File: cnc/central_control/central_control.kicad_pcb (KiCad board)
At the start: 2 copper layers, 64 x 107 mm, 113 parts, among them J1 DE9_Receptacle, J2 AVR-UPDI, J3 7pins, J4 Phoenix, J5 6pins, J6 6pins, J7 6pins, J8 3pins, J9 4pins, Q1 BSS138, U1 ATtiny1626-S, U10 PC817, U2 PC817, U3 PC817, U4 PCA9555PW, U5 LT1785AxS8, U7 LMR33630ADDA, U8 PC817, U9 PCA9555PW

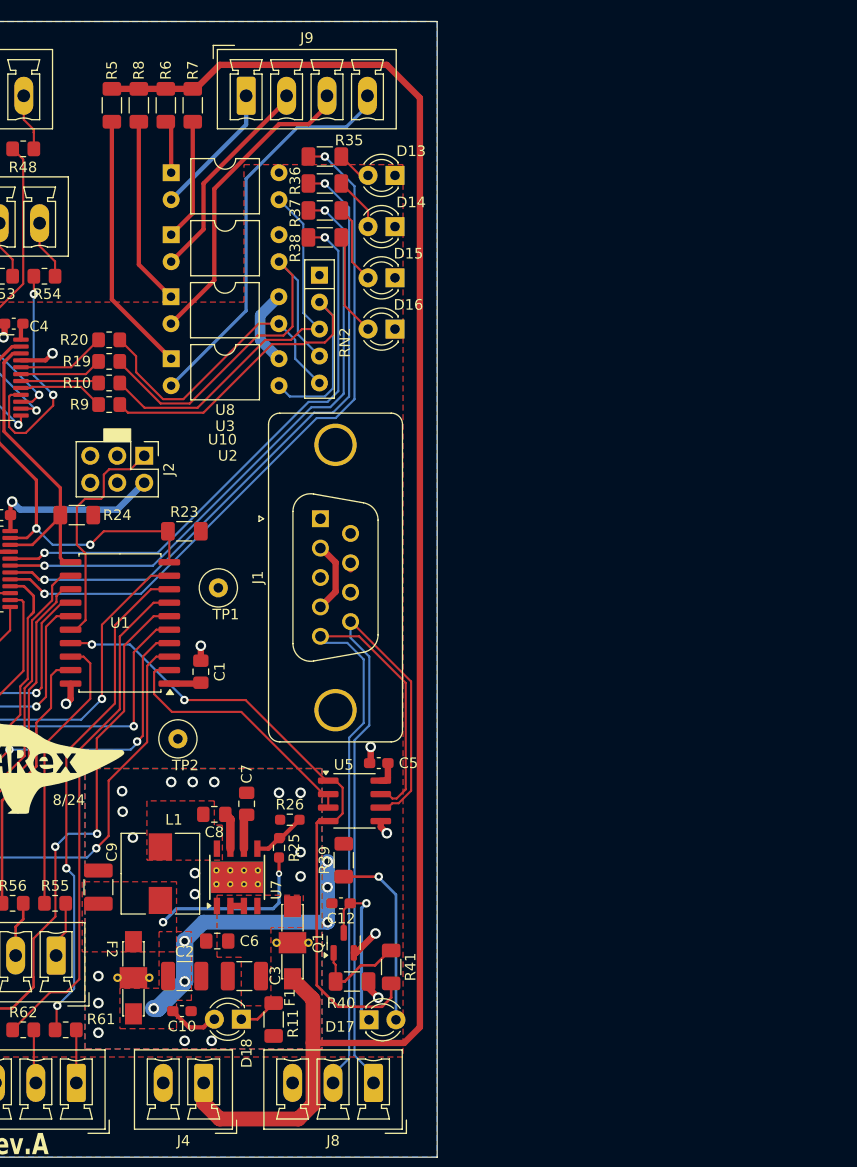
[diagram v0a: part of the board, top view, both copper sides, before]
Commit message: Split sheets
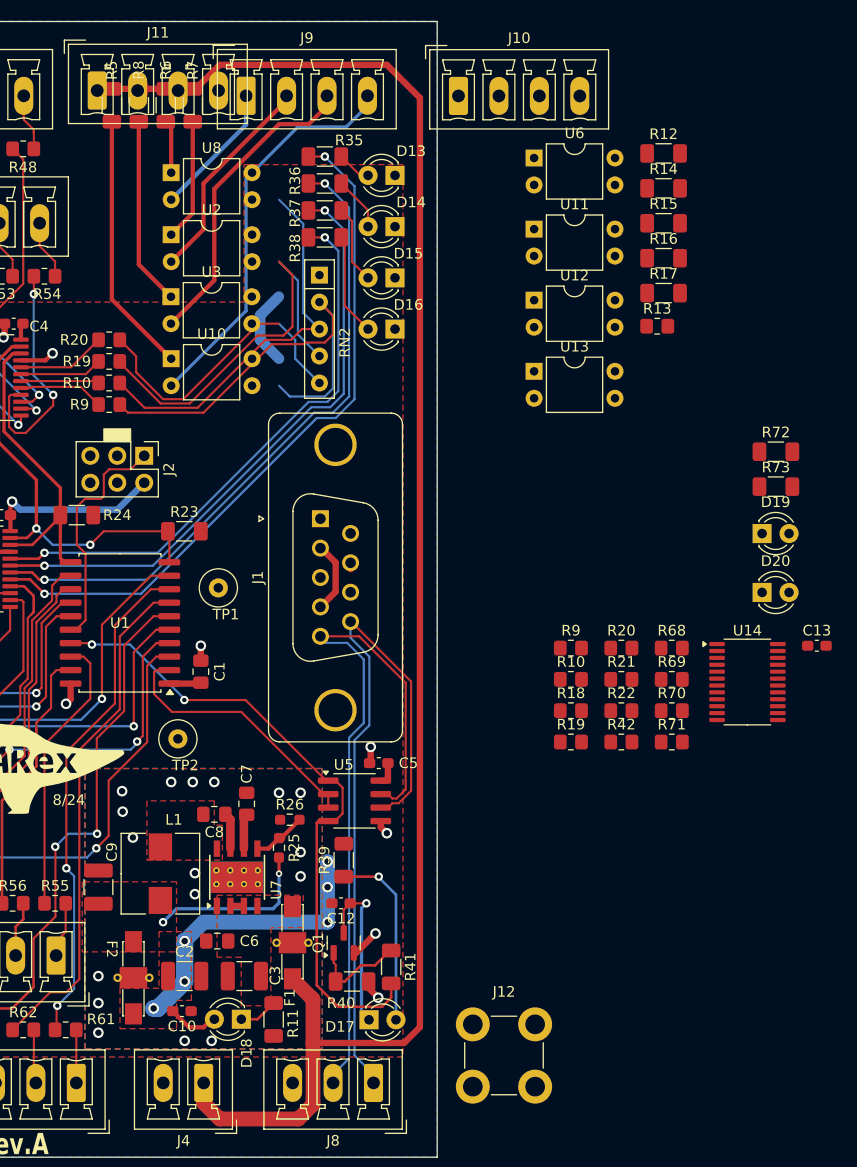
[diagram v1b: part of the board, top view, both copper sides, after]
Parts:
- added C13: 100n, Capacitor_SMD:C_0603_1608Metric_Pad1.08x0.95mm_HandSolder, F.Cu at (199.8, 107.8)
- added D19: LED, LED_THT:LED_D3.0mm, F.Cu at (194.6, 97.2)
- added D20: LED, LED_THT:LED_D3.0mm, F.Cu at (194.6, 102.8)
- added J10: 4pins, Connector_Phoenix_MC:PhoenixContact_MCV_1,5_4-G-3.81_1x04_P3.81mm_Vertical, F.Cu at (166.0, 56.0)
- added J11: Screw_Terminal_01x04, Connector_Phoenix_MC:PhoenixContact_MCV_1,5_4-G-3.81_1x04_P3.81mm_Vertical, F.Cu at (132.0, 55.5)
- added J12: Screw_Terminal_01x01, TerminalBlock_Wuerth:Wuerth_REDCUBE-THR_WP-THRBU_74650173_THR, F.Cu at (170.3, 146.4)
- added R10: 332, Resistor_SMD:R_0805_2012Metric_Pad1.20x1.40mm_HandSolder, F.Cu at (176.6, 111.0)
- added R12: 100K, Resistor_SMD:R_1206_3216Metric_Pad1.30x1.75mm_HandSolder, F.Cu at (185.3, 61.4)
- added R13: 332, Resistor_SMD:R_0805_2012Metric_Pad1.20x1.40mm_HandSolder, F.Cu at (184.7, 77.7)
- added R14: 3k32, Resistor_SMD:R_1206_3216Metric_Pad1.30x1.75mm_HandSolder, F.Cu at (185.3, 64.7)
- added R15: 3k32, Resistor_SMD:R_1206_3216Metric_Pad1.30x1.75mm_HandSolder, F.Cu at (185.3, 68.0)
- added R16: 3k32, Resistor_SMD:R_1206_3216Metric_Pad1.30x1.75mm_HandSolder, F.Cu at (185.3, 71.3)
- added R17: 3k32, Resistor_SMD:R_1206_3216Metric_Pad1.30x1.75mm_HandSolder, F.Cu at (185.3, 74.6)
- added R18: 332, Resistor_SMD:R_0805_2012Metric_Pad1.20x1.40mm_HandSolder, F.Cu at (176.6, 113.9)
- added R19: 332, Resistor_SMD:R_0805_2012Metric_Pad1.20x1.40mm_HandSolder, F.Cu at (176.6, 116.9)
- added R20: 332, Resistor_SMD:R_0805_2012Metric_Pad1.20x1.40mm_HandSolder, F.Cu at (181.4, 108.0)
- added R21: 332, Resistor_SMD:R_0805_2012Metric_Pad1.20x1.40mm_HandSolder, F.Cu at (181.4, 111.0)
- added R22: 332, Resistor_SMD:R_0805_2012Metric_Pad1.20x1.40mm_HandSolder, F.Cu at (181.4, 113.9)
- added R42: 332, Resistor_SMD:R_0805_2012Metric_Pad1.20x1.40mm_HandSolder, F.Cu at (181.4, 116.9)
- added R68: 332, Resistor_SMD:R_0805_2012Metric_Pad1.20x1.40mm_HandSolder, F.Cu at (186.1, 108.0)
- added R69: 332, Resistor_SMD:R_0805_2012Metric_Pad1.20x1.40mm_HandSolder, F.Cu at (186.1, 111.0)
- added R70: 332, Resistor_SMD:R_0805_2012Metric_Pad1.20x1.40mm_HandSolder, F.Cu at (186.1, 113.9)
- added R71: 332, Resistor_SMD:R_0805_2012Metric_Pad1.20x1.40mm_HandSolder, F.Cu at (186.1, 116.9)
- added R72: 432, Resistor_SMD:R_1206_3216Metric_Pad1.30x1.75mm_HandSolder, F.Cu at (195.9, 89.5)
- added R73: 432, Resistor_SMD:R_1206_3216Metric_Pad1.30x1.75mm_HandSolder, F.Cu at (195.9, 92.8)
- added R9: 332, Resistor_SMD:R_0805_2012Metric_Pad1.20x1.40mm_HandSolder, F.Cu at (176.6, 108.0)
- added U11: PC817, Package_DIP:DIP-4_W7.62mm, F.Cu at (173.1, 68.6)
- added U12: PC817, Package_DIP:DIP-4_W7.62mm, F.Cu at (173.1, 75.3)
- added U13: PC817, Package_DIP:DIP-4_W7.62mm, F.Cu at (173.1, 82.0)
- added U14: PCA9555PW, Package_SO:TSSOP-24_4.4x7.8mm_P0.65mm, F.Cu at (193.2, 111.2)
- added U6: PC817, Package_DIP:DIP-4_W7.62mm, F.Cu at (173.1, 61.9)
- U10, U2, U3, U8: footprint Package_DIP:DIP-4_W10.16mm -> Package_DIP:DIP-4_W7.62mm
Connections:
- net /VIN renamed /VDD
- J1 pad 2: VDD -> +24V
- J1 pad 4: VDD -> +24V
- U1 pad 12: /MSO_OUT9 -> Net-(U1-PC0)
- U1 pad 13: /MSO_OUT10 -> Net-(U1-PC1)
- U1 pad 14: /MSO_OUT11 -> Net-(U1-PC2)
- U1 pad 15: /MSO_OUT12 -> Net-(U1-PC3)
- U1 pad 17: TXD -> Net-(U1-PA1)
- U1 pad 18: /MSO_OUT0 -> Net-(U1-PA2)
- U1 pad 19: /MSO_OUT1 -> Net-(U1-PA3)
- U1 pad 3: /MSO_OUT2 -> unconnected-(U1-PA5-Pad3)
- U1 pad 4: /MSO_OUT3 -> unconnected-(U1-PA6-Pad4)
- U1 pad 5: /MSO_OUT4 -> unconnected-(U1-PA7-Pad5)
- U1 pad 6: /MSO_OUT8 -> Net-(U1-PB5)
- U1 pad 7: /MSO_OUT7 -> Net-(U1-PB4)
- U1 pad 8: /MSO_OUT6 -> Net-(U1-PB3)
- U1 pad 9: /MSO_OUT5 -> Net-(U1-PB2)
- U4 pad 17: Net-(U4-IO1_4) -> unconnected-(U4-IO1_4-Pad17)
- U4 pad 18: Net-(U4-IO1_5) -> unconnected-(U4-IO1_5-Pad18)
- U4 pad 19: Net-(U4-IO1_6) -> unconnected-(U4-IO1_6-Pad19)
- U4 pad 20: Net-(U4-IO1_7) -> unconnected-(U4-IO1_7-Pad20)
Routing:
- net DOOR_DOWN: track 28.3 -> 35.6 mm
- net VCC: track 63.4 -> 56.1 mm
- net +24V: track 155.2 -> 161.9 mm
- net VDD: track 6.69 -> 0.00 mm

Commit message: On-going
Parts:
- removed C11: 100n, Capacitor_SMD:C_0603_1608Metric_Pad1.08x0.95mm_HandSolder
- removed D19, D20: LED, LED_THT:LED_D3.0mm
- removed J3: 7pins, Connector_Phoenix_MC:PhoenixContact_MCV_1,5_7-G-3.81_1x07_P3.81mm_Vertical
- removed J4: Phoenix, Connector_Phoenix_MC:PhoenixContact_MCV_1,5_2-G-3.81_1x02_P3.81mm_Vertical
- removed J5: 6pins, Connector_Phoenix_MC:PhoenixContact_MCV_1,5_6-G-3.81_1x06_P3.81mm_Vertical
- removed J9: 4pins, Connector_Phoenix_MC:PhoenixContact_MCV_1,5_4-G-3.81_1x04_P3.81mm_Vertical
- removed Q1: BSS138, Package_TO_SOT_SMD:SOT-23
- removed R23: 2k21, Resistor_SMD:R_1206_3216Metric_Pad1.30x1.75mm_HandSolder
- removed R73: 432, Resistor_SMD:R_1206_3216Metric_Pad1.30x1.75mm_HandSolder
- removed RN2: R_Network04, Resistor_THT:R_Array_SIP5
- removed U14, U4: PCA9555PW, Package_SO:TSSOP-24_4.4x7.8mm_P0.65mm
- added C14: 100n, Capacitor_SMD:C_0603_1608Metric_Pad1.08x0.95mm_HandSolder, F.Cu at (385.7, 167.1)
- added J13: 3pins, Connector_Phoenix_MC:PhoenixContact_MCV_1,5_3-G-3.81_1x03_P3.81mm_Vertical, F.Cu at (177.5, 148.8)
- added J14: DE9_Receptacle, Connector_Dsub:DSUB-9_Socket_Vertical_P2.77x2.84mm_MountingHoles, F.Cu at (192.8, 84.7)
- added J17: Phoenix, Connector_Phoenix_MC:PhoenixContact_MCV_1,5_2-G-3.81_1x02_P3.81mm_Vertical, F.Cu at (134.4, 148.8)
- added J18: Phoenix, Connector_Phoenix_MC:PhoenixContact_MCV_1,5_2-G-3.81_1x02_P3.81mm_Vertical, F.Cu at (130.6, 56.1)
- added J19: 7pins, Connector_Phoenix_MC:PhoenixContact_MCV_1,5_7-G-3.81_1x07_P3.81mm_Vertical, F.Cu at (136.9, 67.8)
- added J20: 3pins, Connector_Phoenix_MC:PhoenixContact_MCV_1,5_3-G-3.81_1x03_P3.81mm_Vertical, F.Cu at (190.2, 56.1)
- added J21: 3pins, Connector_Phoenix_MC:PhoenixContact_MCV_1,5_3-G-3.81_1x03_P3.81mm_Vertical, F.Cu at (176.3, 56.1)
- added J22: Phoenix, Connector_Phoenix_MC:PhoenixContact_MCV_1,5_2-G-3.81_1x02_P3.81mm_Vertical, F.Cu at (166.1, 56.1)
- added J23: 3pins, Connector_Phoenix_MC:PhoenixContact_MCV_1,5_3-G-3.81_1x03_P3.81mm_Vertical, F.Cu at (166.1, 67.8)
- added J24: 3pins, Connector_Phoenix_MC:PhoenixContact_MCV_1,5_3-G-3.81_1x03_P3.81mm_Vertical, F.Cu at (122.9, 67.8)
- added RN1: 10k, Resistor_THT:R_Array_SIP5, F.Cu at (361.9, 168.0)
- added TP3: IDLE, TestPoint:TestPoint_Loop_D3.50mm_Drill0.9mm_Beaded, F.Cu at (378.9, 168.5)
- C1: value 1u -> 10u 50v; footprint Capacitor_SMD:C_0805_2012Metric_Pad1.18x1.45mm_HandSolder -> Capacitor_SMD:C_1210_3225Metric_Pad1.33x2.70mm_HandSolder
- C10: value 100n -> 1u; footprint Capacitor_SMD:C_0603_1608Metric_Pad1.08x0.95mm_HandSolder -> Capacitor_SMD:C_0805_2012Metric_Pad1.18x1.45mm_HandSolder
- C12: value 1u -> 100n
- C2: value 47u -> 220nF; footprint Capacitor_SMD:C_1210_3225Metric_Pad1.33x2.70mm_HandSolder -> Capacitor_SMD:C_0805_2012Metric_Pad1.18x1.45mm_HandSolder
- C3: value 10u 50v -> 1u; footprint Capacitor_SMD:C_1210_3225Metric_Pad1.33x2.70mm_HandSolder -> Capacitor_SMD:C_0805_2012Metric_Pad1.18x1.45mm_HandSolder
- C4: value 100n -> 10n; footprint Capacitor_SMD:C_0603_1608Metric_Pad1.08x0.95mm_HandSolder -> Capacitor_SMD:C_0805_2012Metric_Pad1.18x1.45mm_HandSolder
- C5: value 100n -> 10u 50v; footprint Capacitor_SMD:C_0603_1608Metric_Pad1.08x0.95mm_HandSolder -> Capacitor_SMD:C_1210_3225Metric_Pad1.33x2.70mm_HandSolder
- C6: value 220nF -> 47u; footprint Capacitor_SMD:C_0805_2012Metric_Pad1.18x1.45mm_HandSolder -> Capacitor_SMD:C_1210_3225Metric_Pad1.33x2.70mm_HandSolder
- C7: value 1u -> 100n; footprint Capacitor_SMD:C_0805_2012Metric_Pad1.18x1.45mm_HandSolder -> Capacitor_SMD:C_0603_1608Metric_Pad1.08x0.95mm_HandSolder
- C8: value 10n -> 100n; footprint Capacitor_SMD:C_0805_2012Metric_Pad1.18x1.45mm_HandSolder -> Capacitor_SMD:C_0603_1608Metric_Pad1.08x0.95mm_HandSolder
- C9: value 10u 50v -> 100n; footprint Capacitor_SMD:C_1210_3225Metric_Pad1.33x2.70mm_HandSolder -> Capacitor_SMD:C_0805_2012Metric_Pad1.18x1.45mm_HandSolder
- D2: value LED -> red
- D3: value LED -> orange
- D4: value LED -> green
- D5: value LED -> GRN
- J1: value DE9_Receptacle -> AVR-UPDI; footprint Connector_Dsub:DSUB-9_Female_Vertical_P2.77x2.84mm_MountingHoles -> Connector_PinHeader_2.54mm:PinHeader_2x03_P2.54mm_Vertical
- J10: value 4pins -> Screw_Terminal_01x01; footprint Connector_Phoenix_MC:PhoenixContact_MCV_1,5_4-G-3.81_1x04_P3.81mm_Vertical -> adarwoo:GroundPlot
- J11: value Screw_Terminal_01x04 -> 6pins; footprint Connector_Phoenix_MC:PhoenixContact_MCV_1,5_4-G-3.81_1x04_P3.81mm_Vertical -> Connector_Phoenix_MC:PhoenixContact_MCV_1,5_6-G-3.81_1x06_P3.81mm_Vertical
- J12: value Screw_Terminal_01x01 -> 7pins; footprint TerminalBlock_Wuerth:Wuerth_REDCUBE-THR_WP-THRBU_74650173_THR -> Connector_Phoenix_MC:PhoenixContact_MCV_1,5_7-G-3.81_1x07_P3.81mm_Vertical
- J2: value AVR-UPDI -> Screw_Terminal_01x04; footprint Connector_PinHeader_2.54mm:PinHeader_2x03_P2.54mm_Vertical -> Connector_Phoenix_MC:PhoenixContact_MCV_1,5_4-G-3.81_1x04_P3.81mm_Vertical
- J6: value 6pins -> Phoenix; footprint Connector_Phoenix_MC:PhoenixContact_MCV_1,5_6-G-3.81_1x06_P3.81mm_Vertical -> Connector_Phoenix_MC:PhoenixContact_MCV_1,5_2-G-3.81_1x02_P3.81mm_Vertical
- J8: value 3pins -> 6pins; footprint Connector_Phoenix_MC:PhoenixContact_MCV_1,5_3-G-3.81_1x03_P3.81mm_Vertical -> Connector_Phoenix_MC:PhoenixContact_MCV_1,5_6-G-3.81_1x06_P3.81mm_Vertical
- R1: value 432 -> 100k; footprint Resistor_SMD:R_1206_3216Metric_Pad1.30x1.75mm_HandSolder -> Resistor_SMD:R_0603_1608Metric_Pad0.98x0.95mm_HandSolder
- R10 (x2), R13, R18, R19 (x2), R44, R45, R46, R47, R48, R49, R50, R51, R52, R53, R54, R55, R56, R57, R58, R59, R60, R61, R62, R63, R64, R65, R66, R67, R68, R69, R70, R71, R9 (x2): footprint Resistor_SMD:R_0805_2012Metric_Pad1.20x1.40mm_HandSolder -> Resistor_SMD:R_1206_3216Metric_Pad1.30x1.75mm_HandSolder
- R11: value 680 -> 332
- R12: value 100K -> 332
- R14, R15, R16, R17, R7, R8: value 3k32 -> 332
- R2: value 432 -> 24k9; footprint Resistor_SMD:R_1206_3216Metric_Pad1.30x1.75mm_HandSolder -> Resistor_SMD:R_0603_1608Metric_Pad0.98x0.95mm_HandSolder
- R20 (x2), R21, R22, R42, R43: value 332 -> 432; footprint Resistor_SMD:R_0805_2012Metric_Pad1.20x1.40mm_HandSolder -> Resistor_SMD:R_1206_3216Metric_Pad1.30x1.75mm_HandSolder
- R24: value 2k21 -> 3k32
- R25: value 100k -> 3k32; footprint Resistor_SMD:R_0603_1608Metric_Pad0.98x0.95mm_HandSolder -> Resistor_SMD:R_1206_3216Metric_Pad1.30x1.75mm_HandSolder
- R26: value 24k9 -> 3k32; footprint Resistor_SMD:R_0603_1608Metric_Pad0.98x0.95mm_HandSolder -> Resistor_SMD:R_1206_3216Metric_Pad1.30x1.75mm_HandSolder
- R27, R28, R29: value 432 -> 3k32
- R3: value 432 -> 680
- R39: value 680 -> 432
- R4: value 432 -> 100K
- R40: value 100K -> 432
- R41: value 100 -> 432
- R5, R6: value 3k32 -> 6k81
- R72: value 432 -> 332
- TP1: value TestPoint -> Vcc TP
- TP2: value TestPoint -> GND_TP
- U1: value ATtiny1626-S -> LMR33630ADDA; footprint Package_SO:SOIC-20W_7.5x12.8mm_P1.27mm -> Package_SO:Texas_HSOP-8-1EP_3.9x4.9mm_P1.27mm_ThermalVias
- U11, U12, U13: value PC817 -> PCA9555PW; footprint Package_DIP:DIP-4_W7.62mm -> Package_SO:TSSOP-24_4.4x7.8mm_P0.65mm
- U2: value PC817 -> LT1785AxS8; footprint Package_DIP:DIP-4_W7.62mm -> Package_SO:SOIC-8_3.9x4.9mm_P1.27mm
- U3: value PC817 -> ATtiny3226; footprint Package_DIP:DIP-4_W7.62mm -> Package_SO:SOIC-20W_7.5x12.8mm_P1.27mm
- U5: value LT1785AxS8 -> PC817; footprint Package_SO:SOIC-8_3.9x4.9mm_P1.27mm -> Package_DIP:DIP-4_W7.62mm
- U7: value LMR33630ADDA -> PC817; footprint Package_SO:Texas_HSOP-8-1EP_3.9x4.9mm_P1.27mm_ThermalVias -> Package_DIP:DIP-4_W7.62mm
- U9: value PCA9555PW -> PC817; footprint Package_SO:TSSOP-24_4.4x7.8mm_P0.65mm -> Package_DIP:DIP-4_W7.62mm
- moved R43 281.2 mm to (371.1, 151.8), turned to 90 degrees
- moved R28 273.6 mm to (383.0, 118.6)
- moved U9 263.6 mm to (384.0, 116.2), turned to 90 degrees
- moved U2 262.7 mm to (388.0, 152.6)
- moved R8 257.0 mm to (370.6, 161.5)
- moved U8 256.1 mm to (389.5, 116.2), turned to 90 degrees
- moved U1 245.9 mm to (378.8, 130.3), turned to -90 degrees
- moved D2 241.5 mm to (340.0, 130.7)
- moved U10 236.7 mm to (373.0, 116.2), turned to 90 degrees
- moved R9 233.8 mm to (360.0, 141.7)
- moved C3 233.6 mm to (379.5, 139.8)
- moved F1 233.6 mm to (384.0, 136.7)
- moved C2 233.6 mm to (373.8, 139.8)
- moved C6 233.6 mm to (376.9, 136.5)
- moved C9 233.6 mm to (365.7, 131.5)
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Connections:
- net /MSO_OUT0 renamed /Connections/MSO_IN11
- net /MSO_OUT5 renamed /Connections/MSO_OUT_TO_IN_1
- C1 pad 1: VCC -> VDD
- C1 pad 2: GND -> Earth
- C10 pad 1: GND -> VCC
- C10 pad 2: VCC -> Earth
- C12 pad 1: Net-(D17-K) -> VCC
- C12 pad 2: VCC -> Earth
- C13 pad 2: GND -> Earth
- C2 pad 1: VCC -> VDD
- C2 pad 2: GND -> Earth
- C3 pad 1: /VDD -> Net-(U1-VCC)
- C3 pad 2: GND -> Earth
- C4 pad 1: VCC -> Net-(U1-BOOT)
- C4 pad 2: GND -> Net-(U1-SW)
- C5 pad 1: GND -> Net-(C5-Pad1)
- C5 pad 2: VCC -> Earth
- C6 pad 1: /VDD -> VCC
- C6 pad 2: GND -> Earth
- C7 pad 1: Net-(U7-VCC) -> Earth
- C7 pad 2: GND -> VCC
- C8 pad 1: Net-(U7-BOOT) -> Earth
- C8 pad 2: Net-(U7-SW) -> VCC
- C9 pad 1: Net-(C9-Pad1) -> VCC
- C9 pad 2: GND -> Earth
- D1 pad 1: GND -> Net-(D1-K)
- D1 pad 2: Net-(D1-A) -> VCC
- D10 pad 1: GND -> Earth
- D11 pad 1: GND -> Earth
- D12 pad 1: GND -> Earth
- D13 pad 1: GND -> Earth
- D14 pad 1: GND -> Earth
- D15 pad 1: GND -> Earth
- D16 pad 1: GND -> Earth
- D17 pad 1: Net-(D17-K) -> Earth
- D18 pad 1: Net-(D18-K) -> Earth
- D18 pad 2: VCC -> Net-(D18-A)
- D2 pad 1: GND -> Earth
- D3 pad 1: GND -> Earth
- D4 pad 1: GND -> Earth
- D5 pad 1: GND -> Earth
- D6 pad 1: GND -> Earth
- D7 pad 1: GND -> Earth
- D8 pad 1: GND -> Earth
- D9 pad 1: GND -> Earth
- F1 pad 2: GND -> Earth
- F1 pad 3: /VDD -> VDD
- F2 pad 1: Net-(C9-Pad1) -> Net-(C5-Pad1)
- F2 pad 2: GND -> Earth
- J1 pad 1: GND -> UPDI
- J1 pad 2: +24V -> VCC
- J1 pad 4: +24V -> unconnected-(J1-NC-Pad4)
- J1 pad 5: RS+ -> unconnected-(J1-NC-Pad5)
- J1 pad 6: GND -> Earth
- J10 pad 1: OC_OUT0 -> Earth
- J12 pad 1: Earth -> Net-(J12-Pin_1)
- J2 pad 1: UPDI -> unconnected-(J2-Pin_1-Pad1)
- J2 pad 2: VCC -> unconnected-(J2-Pin_2-Pad2)
- J6 pad 1: Net-(J6-Pin_1) -> +24V
- J6 pad 2: Net-(J6-Pin_2) -> Earth
- J8 pad 1: RS- -> Net-(J8-Pin_1)
- J8 pad 2: RS+ -> Net-(J8-Pin_2)
- J8 pad 3: GND -> Net-(J8-Pin_3)
- L1 pad 1: Net-(U7-SW) -> Net-(U1-SW)
- L1 pad 2: Net-(C9-Pad1) -> Net-(C5-Pad1)
- R1 pad 1: Net-(U9-IO0_0) -> Net-(U1-FB)
- R1 pad 2: Net-(D1-A) -> Net-(C5-Pad1)
- R10 pad 1: OU1 -> ISO_OUT_RELEASE_STEPPERS
- R10 pad 2: Net-(U1-PC1) -> Net-(U3-PC3)
- R10 pad 1: Net-(U4-IO1_5) -> ISO_OUT_RELEASE_STEPPERS
- R10 pad 2: SPINDLE_ON -> Net-(U3-PC3)
- R11 pad 1: GND -> Net-(U3-TxD)
- R11 pad 2: Net-(D18-K) -> RTXD
- R12 pad 1: GND -> Net-(U3-PA2)
- R12 pad 2: XDIR -> IDLE
- R13 pad 1: Net-(U1-PA1) -> Net-(U3-XDIR)
- R13 pad 2: TXD -> XDIR
- R14 pad 1: Net-(R14-Pad1) -> Net-(U3-PB0)
- R14 pad 2: GND -> SCL
- R15 pad 1: Net-(R15-Pad1) -> Net-(U3-PB1)
- R15 pad 2: GND -> SDA
- R16 pad 1: Net-(R16-Pad1) -> Net-(U3-PB2)
- R16 pad 2: GND -> ISO_IN_SPARE_0
- R17 pad 1: Net-(R17-Pad1) -> Net-(U3-PB3)
- R17 pad 2: GND -> ISO_IN_SPINDLE_IS_ON
- R18 pad 1: Net-(U1-PB2) -> Net-(U3-PB4)
- R18 pad 2: SPARE -> ISO_IN_DOOR_IS_UP
- R19 pad 1: OUT2 -> Net-(U3-PB5)
- R19 pad 2: Net-(U1-PC2) -> ISO_IN_DOOR_IS_DOWN
- R19 pad 1: Net-(U4-IO1_6) -> Net-(U3-PB5)
- R19 pad 2: DOOR_UP -> ISO_IN_DOOR_IS_DOWN
- R2 pad 1: Net-(U9-IO0_1) -> Earth
- R2 pad 2: Net-(D2-A) -> Net-(U1-FB)
- R20 pad 1: Net-(U4-IO1_7) -> TRACE_ERR
- R20 pad 2: DOOR_DOWN -> Net-(D2-A)
- R20 pad 1: OUT3 -> TRACE_ERR
- R20 pad 2: Net-(U1-PC3) -> Net-(D2-A)
- R21 pad 1: Net-(U1-PB3) -> RS_TX_PULSE
- R21 pad 2: SPINDLE_ON -> Net-(D3-A)
- R22 pad 1: Net-(U1-PB4) -> RS_RX_PULSE
- R22 pad 2: DOOR_UP -> Net-(D4-A)
- R24 pad 1: SCL -> Earth
- R24 pad 2: VCC -> Net-(R24-Pad2)
- R25 pad 1: Net-(U7-FB) -> Earth
- R25 pad 2: Net-(C9-Pad1) -> Net-(R25-Pad2)
- R26 pad 1: GND -> Net-(R26-Pad1)
- R26 pad 2: Net-(U7-FB) -> +24V
- R27 pad 1: Net-(U9-IO0_4) -> Net-(R27-Pad1)
- R27 pad 2: Net-(D5-A) -> +24V
- R28 pad 1: Net-(U9-IO0_5) -> Net-(R28-Pad1)
- R28 pad 2: Net-(D6-A) -> +24V
- R29 pad 1: Net-(U9-IO0_6) -> Net-(R29-Pad1)
- R29 pad 2: Net-(D7-A) -> +24V
- R3 pad 1: Net-(U9-IO0_2) -> Earth
- R3 pad 2: Net-(D3-A) -> Net-(D1-K)
- R30 pad 1: Net-(U9-IO0_7) -> Net-(U11-IO0_0)
- R30 pad 2: Net-(D8-A) -> Net-(D5-A)
- R31 pad 1: Net-(U9-IO1_0) -> Net-(U11-IO0_1)
- R31 pad 2: Net-(D9-A) -> Net-(D6-A)
- R32 pad 1: Net-(U9-IO1_1) -> Net-(U11-IO0_2)
- R32 pad 2: Net-(D10-A) -> Net-(D7-A)
- R33 pad 1: Net-(U9-IO1_2) -> Net-(U11-IO0_3)
- R33 pad 2: Net-(D11-A) -> Net-(D8-A)
- R34 pad 1: Net-(U9-IO1_3) -> Net-(U11-IO0_4)
- R34 pad 2: Net-(D12-A) -> Net-(D9-A)
- R35 pad 1: Net-(U9-IO1_4) -> Net-(U11-IO0_5)
- R35 pad 2: Net-(D13-A) -> Net-(D10-A)
- R36 pad 1: Net-(U9-IO1_5) -> Net-(U11-IO0_6)
- R36 pad 2: Net-(D14-A) -> Net-(D11-A)
- R37 pad 1: Net-(U9-IO1_6) -> Net-(U11-IO1_0)
- R37 pad 2: Net-(D15-A) -> Net-(D12-A)
- R38 pad 1: Net-(U9-IO1_7) -> Net-(U11-IO1_1)
- R38 pad 2: Net-(D16-A) -> Net-(D13-A)
- R39 pad 1: Net-(D17-A) -> Net-(U11-IO1_2)
- R39 pad 2: VCC -> Net-(D14-A)
- R4 pad 1: Net-(U9-IO0_3) -> Earth
- R4 pad 2: Net-(D4-A) -> XDIR
- R40 pad 1: GND -> Net-(U11-IO1_3)
- R40 pad 2: Net-(Q1-G) -> Net-(D15-A)
- R41 pad 1: Net-(Q1-G) -> Net-(U11-IO1_4)
- R41 pad 2: TXD -> Net-(D16-A)
- R42 pad 1: Net-(U1-PB5) -> Net-(U11-IO1_5)
- R42 pad 2: DOOR_DOWN -> Net-(D17-A)
- R43 pad 1: /MSO_IN0 -> Net-(U11-IO1_6)
- R43 pad 2: Net-(J6-Pin_1) -> Net-(D18-A)
- R44 pad 1: /MSO_IN1 -> /Connections/MSO_IN0
- R44 pad 2: Net-(J6-Pin_2) -> Net-(J7-Pin_1)
- R45 pad 1: /MSO_IN2 -> /Connections/MSO_IN1
- R45 pad 2: Net-(J6-Pin_3) -> Net-(J7-Pin_2)
- R46 pad 1: /MSO_IN3 -> /Connections/MSO_IN2
- R46 pad 2: Net-(J6-Pin_4) -> Net-(J7-Pin_3)
- R47 pad 1: /MSO_IN4 -> /Connections/MSO_IN3
- R47 pad 2: Net-(J6-Pin_5) -> Net-(J7-Pin_4)
- R48 pad 1: /MSO_IN5 -> /Connections/MSO_IN4
- R48 pad 2: Net-(J6-Pin_6) -> Net-(J7-Pin_5)
- R49 pad 1: /MSO_IN6 -> /Connections/MSO_IN5
- R49 pad 2: Net-(J7-Pin_1) -> Net-(J7-Pin_6)
- R5 pad 1: Net-(R5-Pad1) -> SDA
- R5 pad 2: +24V -> VCC
- R50 pad 1: /MSO_IN7 -> /Connections/MSO_IN6
- R50 pad 2: Net-(J7-Pin_2) -> Net-(J8-Pin_1)
- R51 pad 1: /MSO_IN8 -> /Connections/MSO_IN7
- R51 pad 2: Net-(J7-Pin_3) -> Net-(J8-Pin_2)
- R52 pad 1: /MSO_IN9 -> /Connections/MSO_IN8
- R52 pad 2: Net-(J7-Pin_4) -> Net-(J8-Pin_3)
- R53 pad 1: /MSO_IN10 -> /Connections/MSO_IN9
- R53 pad 2: Net-(J7-Pin_5) -> Net-(J8-Pin_4)
- R54 pad 1: /MSO_IN11 -> /Connections/MSO_IN10
- R54 pad 2: Net-(J7-Pin_6) -> Net-(J8-Pin_5)
- R55 pad 2: Net-(J5-Pin_1) -> Net-(J8-Pin_6)
- R56 pad 1: /MSO_OUT1 -> unconnected-(R56-Pad1)
- R56 pad 2: Net-(J5-Pin_2) -> unconnected-(R56-Pad2)
- R57 pad 1: /MSO_OUT2 -> unconnected-(R57-Pad1)
- R57 pad 2: Net-(J5-Pin_3) -> unconnected-(R57-Pad2)
- R58 pad 1: /MSO_OUT3 -> unconnected-(R58-Pad1)
- R58 pad 2: Net-(J5-Pin_4) -> unconnected-(R58-Pad2)
- R59 pad 1: /MSO_OUT4 -> unconnected-(R59-Pad1)
- R59 pad 2: Net-(J5-Pin_5) -> unconnected-(R59-Pad2)
- R6 pad 1: Net-(R6-Pad1) -> SCL
- R6 pad 2: +24V -> VCC
- R60 pad 2: Net-(J5-Pin_6) -> Net-(J11-Pin_1)
- R61 pad 1: /MSO_OUT6 -> unconnected-(R61-Pad1)
- R61 pad 2: Net-(J3-Pin_1) -> Net-(J11-Pin_2)
- R62 pad 1: /MSO_OUT7 -> unconnected-(R62-Pad1)
- R62 pad 2: Net-(J3-Pin_2) -> Net-(J11-Pin_3)
- R63 pad 1: /MSO_OUT8 -> unconnected-(R63-Pad1)
- R63 pad 2: Net-(J3-Pin_3) -> Net-(J11-Pin_4)
- R64 pad 1: /MSO_OUT9 -> unconnected-(R64-Pad1)
- R64 pad 2: Net-(J3-Pin_4) -> Net-(J11-Pin_5)
- R65 pad 1: /MSO_OUT10 -> unconnected-(R65-Pad1)
- R65 pad 2: Net-(J3-Pin_5) -> Net-(J11-Pin_6)
- R66 pad 1: /MSO_OUT11 -> unconnected-(R66-Pad1)
- R66 pad 2: Net-(J3-Pin_6) -> Net-(J12-Pin_1)
- R67 pad 1: /MSO_OUT12 -> unconnected-(R67-Pad1)
- R67 pad 2: Net-(J3-Pin_7) -> Net-(J12-Pin_2)
- R68 pad 1: /MSO_IN12 -> unconnected-(R68-Pad1)
- R68 pad 2: Net-(J11-Pin_1) -> Net-(J12-Pin_3)
- R69 pad 1: /MSO_IN13 -> unconnected-(R69-Pad1)
- R69 pad 2: Net-(J11-Pin_2) -> Net-(J12-Pin_4)
- R7 pad 1: Net-(R7-Pad1) -> ISO_OUT_SPARE_0
- R7 pad 2: +24V -> Net-(U3-PC0)
- R70 pad 1: /MSO_IN14 -> unconnected-(R70-Pad1)
- R70 pad 2: Net-(J11-Pin_3) -> Net-(J12-Pin_5)
- R71 pad 1: /MSO_IN15 -> unconnected-(R71-Pad1)
- R71 pad 2: Net-(J11-Pin_4) -> Net-(J12-Pin_6)
- R72 pad 1: Net-(U1-PA2) -> unconnected-(R72-Pad1)
- R72 pad 2: Net-(D19-A) -> Net-(J12-Pin_7)
- R8 pad 1: Net-(R8-Pad1) -> ISO_OUT_SPARE_1
- R8 pad 2: +24V -> Net-(U3-PC1)
- R9 pad 1: OUT0 -> ISO_OUT_SPARE_2
- R9 pad 2: Net-(U1-PC0) -> Net-(U3-PC2)
- R9 pad 1: Net-(U4-IO1_4) -> ISO_OUT_SPARE_2
- R9 pad 2: SPARE -> Net-(U3-PC2)
- TP2 pad 1: GND -> Earth
- U1 pad 1: VCC -> Earth
- U1 pad 2: XDIR -> VDD
- U1 pad 3: unconnected-(U1-PA5-Pad3) -> VDD
- U1 pad 5: unconnected-(U1-PA7-Pad5) -> Net-(U1-FB)
- U1 pad 6: Net-(U1-PB5) -> Net-(U1-VCC)
- U1 pad 7: Net-(U1-PB4) -> Net-(U1-BOOT)
- U1 pad 8: Net-(U1-PB3) -> Net-(U1-SW)
- U1 pad 9: Net-(U1-PB2) -> Earth
- U10 pad 1: Net-(R5-Pad1) -> Net-(R29-Pad1)
- U10 pad 2: SPARE_OC -> OC_IN_DOOR_IS_CLOSED
- U10 pad 3: SPARE -> ISO_IN_DOOR_IS_DOWN
- U11 pad 1: OC_OUT1 -> unconnected-(U11-~{INT}-Pad1)
- U11 pad 2: Net-(R15-Pad1) -> VCC
- U11 pad 3: GND -> Earth
- U11 pad 4: OU1 -> Net-(U11-IO0_0)
- U12 pad 1: OC_OUT2 -> IO_INT
- U12 pad 2: Net-(R16-Pad1) -> Earth
- U12 pad 3: GND -> Earth
- U12 pad 4: OUT2 -> /I2C/MSO_OUT0
- U13 pad 1: OC_OUT3 -> IO_INT
- U13 pad 2: Net-(R17-Pad1) -> Earth
- U13 pad 3: GND -> Earth
- U13 pad 4: OUT3 -> /I2C/MSO_IN0
- U2 pad 1: Net-(R7-Pad1) -> RTXD
- U2 pad 2: DOOR_UP_OC -> XDIR
- U2 pad 3: DOOR_UP -> XDIR
- U2 pad 4: VCC -> RTXD
- U3 pad 1: Net-(R8-Pad1) -> VCC
- U3 pad 2: DOOR_CLOSED_OC -> Net-(U3-XDIR)
- U3 pad 3: DOOR_DOWN -> unconnected-(U3-PA5-Pad3)
- U3 pad 4: VCC -> RS_TX_PULSE
- U5 pad 1: TXD -> ISO_OUT_SPARE_0
- U5 pad 2: XDIR -> Net-(R25-Pad2)
- U5 pad 3: XDIR -> Earth
- U5 pad 4: TXD -> OC_OUT_SPARE_0
- U6 pad 1: OC_OUT0 -> ISO_OUT_RELEASE_STEPPERS
- U6 pad 2: Net-(R14-Pad1) -> Net-(R24-Pad2)
- U6 pad 3: GND -> Earth
- U6 pad 4: OUT0 -> OC_OUT_RELEASE_STEPPERS
- U7 pad 1: GND -> Net-(R26-Pad1)
- U7 pad 2: /VDD -> OC_IN_SPARE
- U7 pad 3: /VDD -> ISO_IN_SPARE
- U7 pad 4: unconnected-(U7-PG-Pad4) -> VCC
- U8 pad 1: Net-(R6-Pad1) -> Net-(R27-Pad1)
- U8 pad 2: SPINDLE_ON_OC -> OC_IN_SPINDLE_IS_ON
- U8 pad 3: SPINDLE_ON -> ISO_IN_SPINDLE_IS_ON
- U9 pad 1: unconnected-(U9-~{INT}-Pad1) -> Net-(R28-Pad1)
- U9 pad 2: VCC -> OC_IN_DOOR_IS_UP
- U9 pad 3: GND -> ISO_IN_DOOR_IS_UP
- U9 pad 4: Net-(U9-IO0_0) -> VCC
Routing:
- net +24V: track 161.9 -> 0.00 mm
- net RS+: track 67.1 -> 0.00 mm
- net Net-(U9-IO1_4): track 66.2 -> 0.00 mm, vias 2 -> 0
- net RS-: track 65.2 -> 0.00 mm
- net Net-(U9-IO1_5): track 61.9 -> 0.00 mm, vias 2 -> 0
- net TXD: track 59.9 -> 0.00 mm, vias 2 -> 0
- net Net-(U9-IO1_6): track 57.7 -> 0.00 mm, vias 2 -> 0
- net /MSO_OUT10: track 56.2 -> 0.00 mm
- net VCC: track 56.1 -> 0.00 mm, vias 7 -> 0
- net /MSO_OUT12: track 54.5 -> 0.00 mm, vias 2 -> 0
- net Net-(U9-IO1_7): track 54.0 -> 0.00 mm, vias 2 -> 0
- net /MSO_OUT11: track 52.3 -> 0.00 mm, vias 2 -> 0
- net /Connections/MSO_OUT_TO_IN_1: track 50.8 -> 0.00 mm, vias 2 -> 0
- net /MSO_OUT8: track 50.4 -> 0.00 mm, vias 2 -> 0
- net /MSO_OUT7: track 48.1 -> 0.00 mm
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- added copper zone on F.Cu, net Net-(U1-SW)
- added copper zone on B.Cu, net Net-(U3-TxD)
- added copper zone on F.Cu, net Net-(U3-TxD)
- added copper zone on F.Cu, net VDD
- removed copper zone on F.Cu, net /VDD
- removed copper zone on B.Cu, net GND
- removed copper zone on F.Cu, net GND
- removed copper zone on F.Cu, net Net-(C9-Pad1)
- removed copper zone on F.Cu, net Net-(U7-SW)
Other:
- board size 64 x 107 mm -> 103 x 107 mm

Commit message: From scratch
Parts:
- removed F1, F2: ~, Adarwoo:Murata_NFM61R
- removed J17, J18, J22: Phoenix, Connector_Phoenix_MC:PhoenixContact_MCV_1,5_2-G-3.81_1x02_P3.81mm_Vertical
- removed J19: 7pins, Connector_Phoenix_MC:PhoenixContact_MCV_1,5_7-G-3.81_1x07_P3.81mm_Vertical
- removed J21, J23, J24: 3pins, Connector_Phoenix_MC:PhoenixContact_MCV_1,5_3-G-3.81_1x03_P3.81mm_Vertical
- removed the R10 at (257.1, 111.8)
- removed the R10 at (357.4, 132.1)
- removed the R19 at (263.0, 111.8)
- removed the R19 at (354.1, 117.3)
- removed the R20 at (346.5, 130.6)
- removed the R20 at (345.2, 136.1)
- removed R24, R25: 3k32, Resistor_SMD:R_1206_3216Metric_Pad1.30x1.75mm_HandSolder
- removed R56, R57, R58, R59: 332, Resistor_SMD:R_1206_3216Metric_Pad1.30x1.75mm_HandSolder
- removed the R9 at (362.2, 148.8)
- removed the R9 at (360.0, 141.7)
- added J15: DE9_Receptacle, Connector_Dsub:DSUB-9_Socket_Vertical_P2.77x2.84mm_MountingHoles, F.Cu at (191.8, 86.1)
- added J16: Supply, Connector_Phoenix_MC:PhoenixContact_MCV_1,5_2-G-3.81_1x02_P3.81mm_Vertical, F.Cu at (187.7, 149.1)
- added J3: Inputs, Connector_Phoenix_MC:PhoenixContact_MCV_1,5_6-G-3.81_1x06_P3.81mm_Vertical, F.Cu at (124.2, 149.1)
- added J4: Inputs, Connector_Phoenix_MC:PhoenixContact_MCV_1,5_7-G-3.81_1x07_P3.81mm_Vertical, F.Cu at (163.6, 149.1)
- added J5: 7pins, Connector_Phoenix_MC:PhoenixContact_MCV_1,5_7-G-3.81_1x07_P3.81mm_Vertical, F.Cu at (161.0, 66.0)
- added J9: GND, Connector_Phoenix_MC:PhoenixContact_MCV_1,5_2-G-3.81_1x02_P3.81mm_Vertical, F.Cu at (130.6, 55.9)
- added R10: 332, Resistor_SMD:R_1206_3216Metric_Pad1.30x1.75mm_HandSolder, F.Cu at (158.8, 109.5)
- added R19: 332, Resistor_SMD:R_1206_3216Metric_Pad1.30x1.75mm_HandSolder, F.Cu at (137.8, 108.5)
- added R20: 432, Resistor_SMD:R_1206_3216Metric_Pad1.30x1.75mm_HandSolder, F.Cu at (158.7, 102.6)
- added R74: 560, Resistor_SMD:R_1206_3216Metric_Pad1.30x1.75mm_HandSolder, F.Cu at (140.9, 88.0)
- added R75: 560, Resistor_SMD:R_1206_3216Metric_Pad1.30x1.75mm_HandSolder, F.Cu at (135.8, 88.0)
- added R76: 560, Resistor_SMD:R_1206_3216Metric_Pad1.30x1.75mm_HandSolder, F.Cu at (130.7, 88.0)
- added R77: 560, Resistor_SMD:R_1206_3216Metric_Pad1.30x1.75mm_HandSolder, F.Cu at (125.7, 88.0)
- added R78: 560, Resistor_SMD:R_1206_3216Metric_Pad1.30x1.75mm_HandSolder, F.Cu at (161.2, 88.0)
- added R79: 560, Resistor_SMD:R_1206_3216Metric_Pad1.30x1.75mm_HandSolder, F.Cu at (120.6, 88.0)
- added R80: 560, Resistor_SMD:R_1206_3216Metric_Pad1.30x1.75mm_HandSolder, F.Cu at (171.0, 88.0)
- added R81: 560, Resistor_SMD:R_1206_3216Metric_Pad1.30x1.75mm_HandSolder, F.Cu at (156.1, 88.0)
- added R9: 332, Resistor_SMD:R_1206_3216Metric_Pad1.30x1.75mm_HandSolder, F.Cu at (158.8, 111.8)
- added U14: PC817, Package_DIP:DIP-4_W7.62mm, F.Cu at (156.1, 84.0)
- added U15: PC817, Package_DIP:DIP-4_W7.62mm, F.Cu at (161.2, 84.0)
- added U16: PC817, Package_DIP:DIP-4_W7.62mm, F.Cu at (125.7, 84.0)
- added U17: PC817, Package_DIP:DIP-4_W7.62mm, F.Cu at (130.7, 84.0)
- added U18: PC817, Package_DIP:DIP-4_W7.62mm, F.Cu at (135.8, 84.0)
- added U19: PC817, Package_DIP:DIP-4_W7.62mm, F.Cu at (140.9, 84.0)
- J1: value AVR-UPDI -> Outputs; footprint Connector_PinHeader_2.54mm:PinHeader_2x03_P2.54mm_Vertical -> Connector_Phoenix_MC:PhoenixContact_MCV_1,5_6-G-3.81_1x06_P3.81mm_Vertical
- J10: value Screw_Terminal_01x01 -> GND; footprint adarwoo:GroundPlot -> Connector_Phoenix_MC:PhoenixContact_MCV_1,5_2-G-3.81_1x02_P3.81mm_Vertical
- J11, J7: value 6pins -> 3pins; footprint Connector_Phoenix_MC:PhoenixContact_MCV_1,5_6-G-3.81_1x06_P3.81mm_Vertical -> Connector_Phoenix_MC:PhoenixContact_MCV_1,5_3-G-3.81_1x03_P3.81mm_Vertical
- J12: value 7pins -> 3pins; footprint Connector_Phoenix_MC:PhoenixContact_MCV_1,5_7-G-3.81_1x07_P3.81mm_Vertical -> Connector_Phoenix_MC:PhoenixContact_MCV_1,5_3-G-3.81_1x03_P3.81mm_Vertical
- J14: value DE9_Receptacle -> Modbus; footprint Connector_Dsub:DSUB-9_Socket_Vertical_P2.77x2.84mm_MountingHoles -> Connector_Phoenix_MC:PhoenixContact_MCV_1,5_3-G-3.81_1x03_P3.81mm_Vertical
- J2: value Screw_Terminal_01x04 -> Outputs; footprint Connector_Phoenix_MC:PhoenixContact_MCV_1,5_4-G-3.81_1x04_P3.81mm_Vertical -> Connector_Phoenix_MC:PhoenixContact_MCV_1,5_6-G-3.81_1x06_P3.81mm_Vertical
- J20: value 3pins -> AVR-UPDI; footprint Connector_Phoenix_MC:PhoenixContact_MCV_1,5_3-G-3.81_1x03_P3.81mm_Vertical -> Connector_PinHeader_2.54mm:PinHeader_2x03_P2.54mm_Vertical
- J6: value Phoenix -> 3pins; footprint Connector_Phoenix_MC:PhoenixContact_MCV_1,5_2-G-3.81_1x02_P3.81mm_Vertical -> Connector_Phoenix_MC:PhoenixContact_MCV_1,5_3-G-3.81_1x03_P3.81mm_Vertical
- J8: value 6pins -> Phoenix; footprint Connector_Phoenix_MC:PhoenixContact_MCV_1,5_6-G-3.81_1x06_P3.81mm_Vertical -> Connector_Phoenix_MC:PhoenixContact_MCV_1,5_2-G-3.81_1x02_P3.81mm_Vertical
- moved D18 273.3 mm to (106.0, 135.0), turned to 0 degrees
- moved R43 259.2 mm to (112.5, 133.0), turned to 180 degrees
- moved C14 250.7 mm to (144.6, 98.6)
- moved U5 249.0 mm to (120.6, 84.0)
- moved R42 245.0 mm to (112.5, 128.0), turned to 180 degrees
- moved U9 240.2 mm to (146.0, 84.0)
- moved R28 239.0 mm to (146.0, 88.0), turned to -90 degrees
- moved R41 238.9 mm to (112.5, 123.0), turned to 180 degrees
- moved R39 234.5 mm to (112.5, 113.0), turned to 180 degrees
- moved R40 234.4 mm to (112.5, 118.0)
- moved R11 226.5 mm to (158.8, 107.2), turned to 0 degrees
- moved D17 225.9 mm to (106.0, 130.0)
- moved RN1 225.8 mm to (157.2, 72.6)
- moved U8 225.5 mm to (166.3, 84.0)
- moved U10 224.3 mm to (151.1, 84.0)
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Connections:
- J1 pad 1: UPDI -> Net-(J1-Pin_1)
- J1 pad 2: VCC -> Net-(J1-Pin_2)
- J1 pad 3: unconnected-(J1-NC-Pad3) -> Net-(J1-Pin_3)
- J1 pad 4: unconnected-(J1-NC-Pad4) -> Net-(J1-Pin_4)
- J1 pad 5: unconnected-(J1-NC-Pad5) -> Net-(J1-Pin_5)
- J1 pad 6: Earth -> Net-(J1-Pin_6)
- J11 pad 1: Net-(J11-Pin_1) -> +24V
- J11 pad 2: Net-(J11-Pin_2) -> +24V
- J11 pad 3: Net-(J11-Pin_3) -> +24V
- J12 pad 1: Net-(J12-Pin_1) -> Earth
- J12 pad 2: Net-(J12-Pin_2) -> Earth
- J12 pad 3: Net-(J12-Pin_3) -> Earth
- J14 pad 1: Earth -> RS-
- J14 pad 2: +24V -> RS+
- J14 pad 3: unconnected-(J14-Pad3) -> Earth
- J2 pad 1: unconnected-(J2-Pin_1-Pad1) -> Net-(J2-Pin_1)
- J2 pad 2: unconnected-(J2-Pin_2-Pad2) -> Net-(J2-Pin_2)
- J2 pad 3: unconnected-(J2-Pin_3-Pad3) -> Net-(J2-Pin_3)
- J2 pad 4: unconnected-(J2-Pin_4-Pad4) -> Net-(J2-Pin_4)
- J20 pad 1: unconnected-(J20-Pin_1-Pad1) -> UPDI
- J20 pad 2: OC_IN_DOOR_IS_CLOSED -> VCC
- J20 pad 3: Earth -> unconnected-(J20-NC-Pad3)
- J6 pad 2: Earth -> OC_IN_DOOR_IS_CLOSED
- J7 pad 1: Net-(J7-Pin_1) -> +24V
- J7 pad 2: Net-(J7-Pin_2) -> OC_IN_DOOR_IS_UP
- J7 pad 3: Net-(J7-Pin_3) -> Earth
- J8 pad 1: Net-(J8-Pin_1) -> OC_IN_SPINDLE_IS_ON
- J8 pad 2: Net-(J8-Pin_2) -> Earth
- R44 pad 2: Net-(J7-Pin_1) -> Net-(J1-Pin_1)
- R45 pad 2: Net-(J7-Pin_2) -> Net-(J1-Pin_2)
- R46 pad 2: Net-(J7-Pin_3) -> Net-(J1-Pin_3)
- R47 pad 2: Net-(J7-Pin_4) -> Net-(J1-Pin_4)
- R48 pad 2: Net-(J7-Pin_5) -> Net-(J1-Pin_5)
- R49 pad 2: Net-(J7-Pin_6) -> Net-(J1-Pin_6)
- R50 pad 2: Net-(J8-Pin_1) -> Net-(J2-Pin_1)
- R51 pad 2: Net-(J8-Pin_2) -> Net-(J2-Pin_2)
- R52 pad 2: Net-(J8-Pin_3) -> Net-(J2-Pin_3)
- R53 pad 2: Net-(J8-Pin_4) -> Net-(J2-Pin_4)
- R54 pad 2: Net-(J8-Pin_5) -> Net-(J2-Pin_5)
- R55 pad 2: Net-(J8-Pin_6) -> Net-(J2-Pin_6)
- R60 pad 2: Net-(J11-Pin_1) -> Net-(J3-Pin_1)
- R61 pad 2: Net-(J11-Pin_2) -> Net-(J3-Pin_2)
- R62 pad 2: Net-(J11-Pin_3) -> Net-(J3-Pin_3)
- R63 pad 2: Net-(J11-Pin_4) -> Net-(J3-Pin_4)
- R64 pad 2: Net-(J11-Pin_5) -> Net-(J3-Pin_5)
- R65 pad 2: Net-(J11-Pin_6) -> Net-(J3-Pin_6)
- R66 pad 2: Net-(J12-Pin_1) -> Net-(J4-Pin_1)
- R67 pad 2: Net-(J12-Pin_2) -> Net-(J4-Pin_2)
- R68 pad 2: Net-(J12-Pin_3) -> Net-(J4-Pin_3)
- R69 pad 2: Net-(J12-Pin_4) -> Net-(J4-Pin_4)
- R70 pad 2: Net-(J12-Pin_5) -> Net-(J4-Pin_5)
- R71 pad 2: Net-(J12-Pin_6) -> Net-(J4-Pin_6)
- R72 pad 2: Net-(J12-Pin_7) -> Net-(J4-Pin_7)
- U5 pad 1: ISO_OUT_SPARE_0 -> Net-(R79-Pad2)
- U5 pad 2: Net-(R25-Pad2) -> Earth
- U5 pad 4: OC_OUT_SPARE_0 -> OC_OUT_CAMERA_LIGHT
- U6 pad 1: ISO_OUT_RELEASE_STEPPERS -> Net-(R80-Pad2)
- U6 pad 2: Net-(R24-Pad2) -> Earth
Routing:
- removed copper zone on F.Cu, net Net-(U1-SW)
- removed copper zone on B.Cu, net Net-(U3-TxD)
- removed copper zone on F.Cu, net Net-(U3-TxD)
- removed copper zone on F.Cu, net VCC
- removed copper zone on F.Cu, net VDD
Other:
- board text removed: "8/24"
